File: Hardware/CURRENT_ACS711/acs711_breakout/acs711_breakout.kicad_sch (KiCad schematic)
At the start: 13 parts, among them J1 Conn_01x01, J2 Conn_01x01, J3 Conn_01x04, U1 ACS711xEXLT-15AB

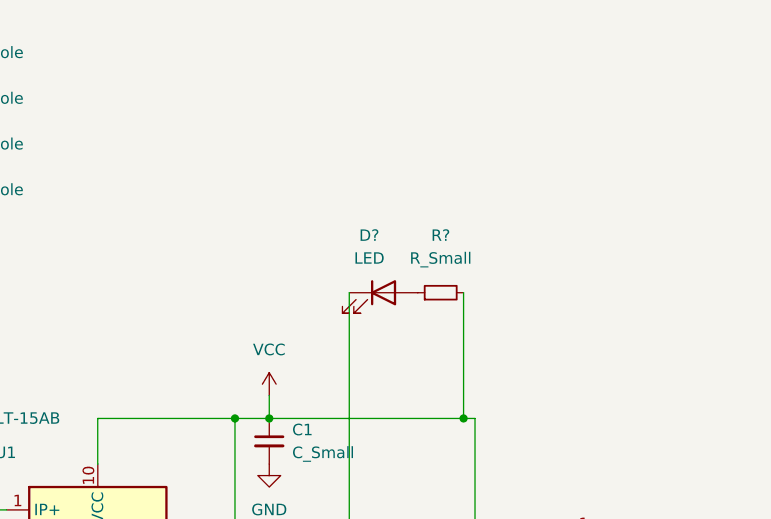
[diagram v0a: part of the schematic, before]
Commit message: layout and some stitching vias
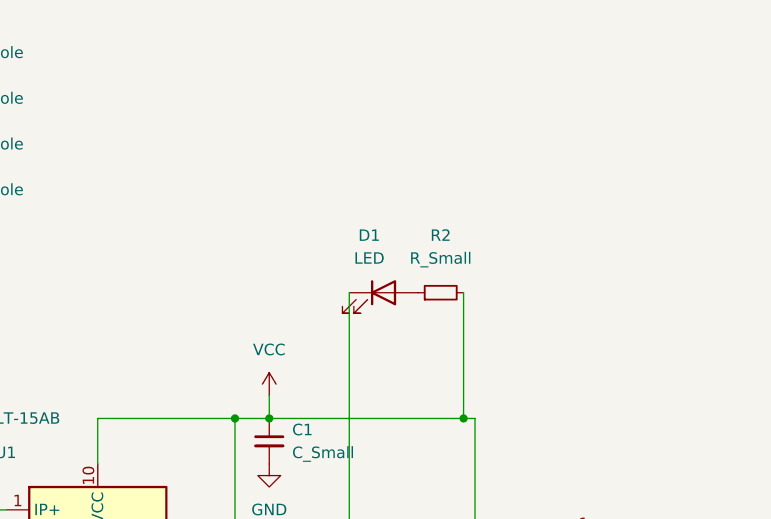
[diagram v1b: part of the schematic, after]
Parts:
- gave numbers to parts that had none: 2
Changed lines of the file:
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@@
   (symbol (lib_id "Device:LED") (at 190.5 62.23 0) (unit 1)
     (in_bom yes) (on_board yes) (fields_autoplaced)
-    (property "Reference" "D?" (id 0) (at 188.9125 55.88 0))
+    (property "Reference" "D1" (id 0) (at 188.9125 55.88 0))
     (property "Value" "LED" (id 1) (at 188.9125 58.42 0))
     (property "Footprint" "LED_SMD:LED_PLCC-2" (id 2) (at 190.5 62.23 0)
@@
   (symbol (lib_id "Device:R_Small") (at 196.85 62.23 90) (unit 1)
     (in_bom yes) (on_board yes) (fields_autoplaced)
-    (property "Reference" "R?" (id 0) (at 196.85 55.88 90))
+    (property "Reference" "R2" (id 0) (at 196.85 55.88 90))
     (property "Value" "R_Small" (id 1) (at 196.85 58.42 90))
     (property "Footprint" "Resistor_SMD:R_0805_2012Metric" (id 2) (at 196.85 62.23 0)
@@
     )
     (path "/af7944d9-46c2-48f3-ab44-3df3aeec04e4"
-      (reference "D?") (unit 1) (value "LED") (footprint "LED_SMD:LED_PLCC-2")
+      (reference "D1") (unit 1) (value "LED") (footprint "LED_SMD:LED_PLCC-2")
     )
     (path "/8c2d72eb-e3f8-4004-bace-d91f46a7cffd"
@@
     )
     (path "/c642f5fe-0d4c-463f-9bd1-b1511f7116d0"
-      (reference "R?") (unit 1) (value "R_Small") (footprint "Resistor_SMD:R_0805_2012Metric")
+      (reference "R2") (unit 1) (value "R_Small") (footprint "Resistor_SMD:R_0805_2012Metric")
     )
     (path "/77d667f7-c52a-418a-9c37-7123db607eaa"

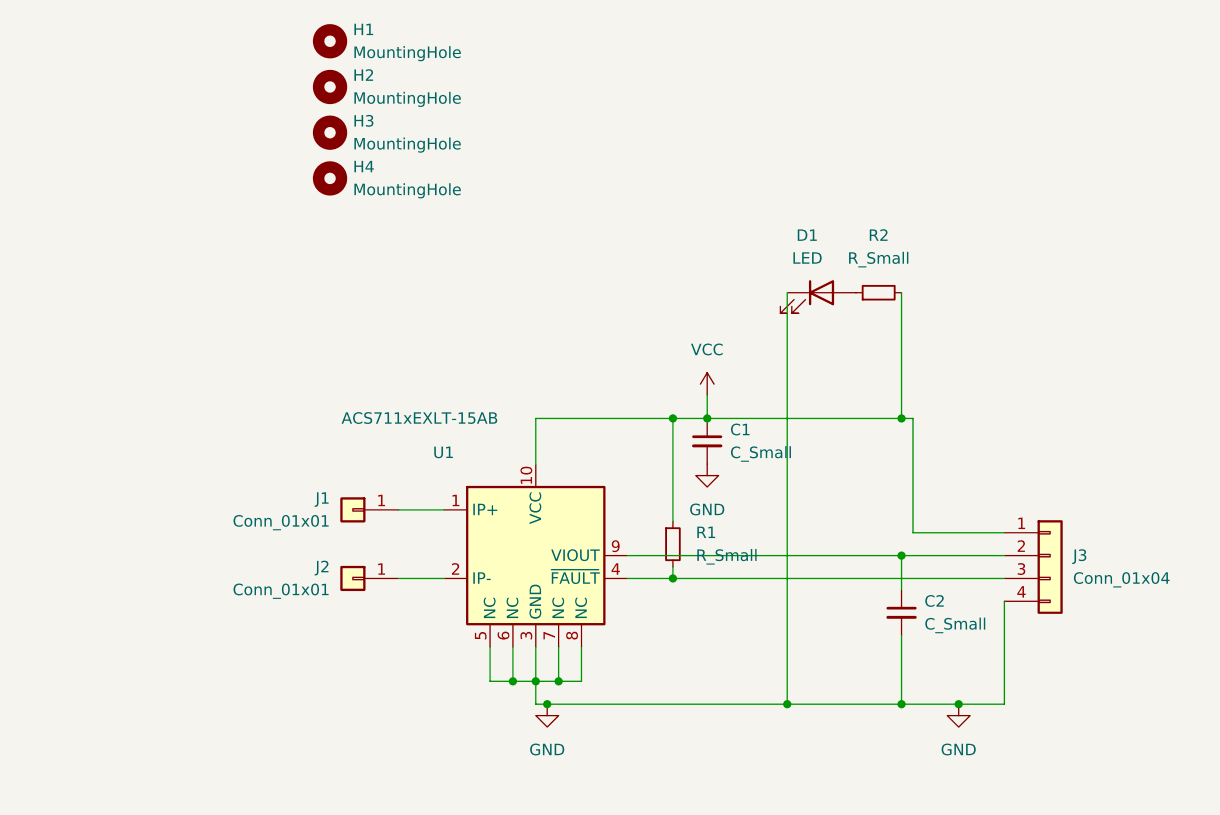
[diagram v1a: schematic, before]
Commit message: Last version of altimeter and ACS7111 pcbs
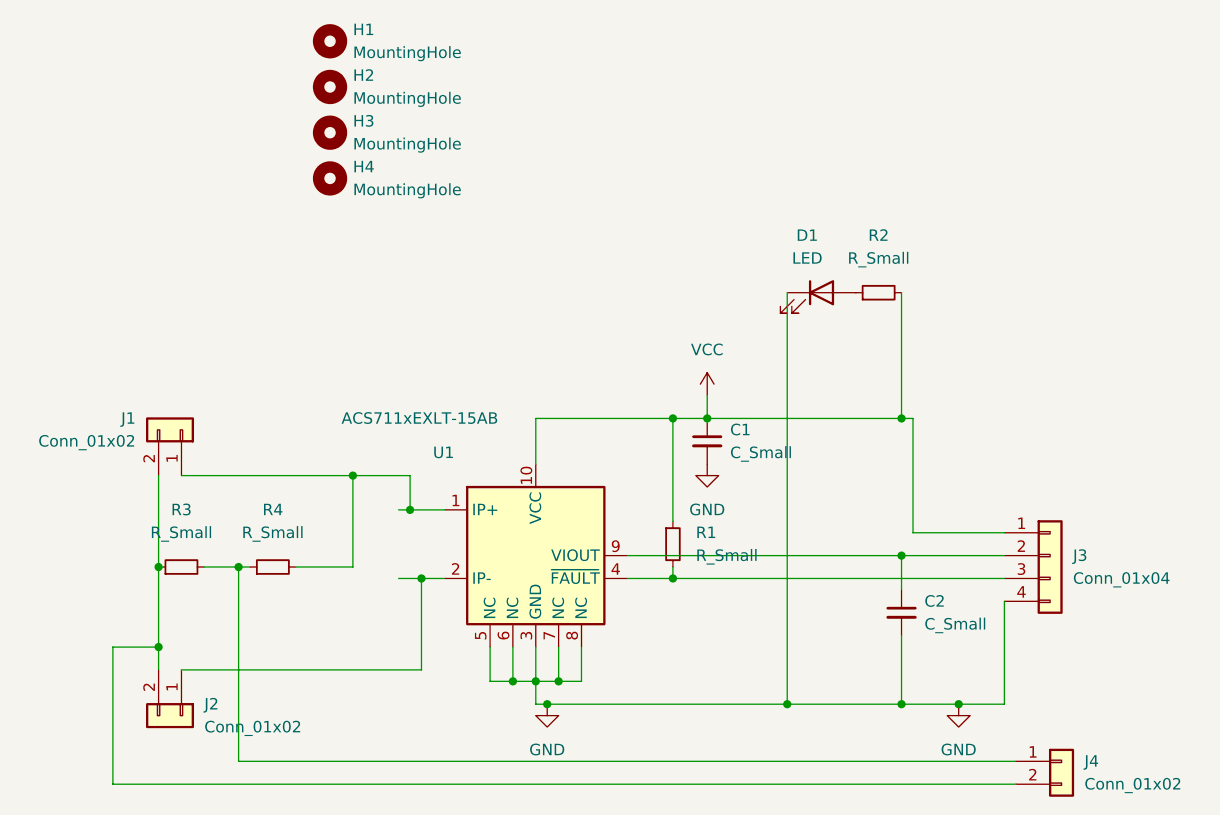
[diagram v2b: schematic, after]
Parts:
- removed J1, J2: Conn_01x01, TestPoint:TestPoint_Pad_4.0x4.0mm, symbol Connector_Generic:Conn_01x01
- added J1: Conn_01x02, Connector_AMASS:AMASS_XT60-M_1x02_P7.20mm_Vertical, symbol Connector_Generic:Conn_01x02
- added J2: Conn_01x02, Connector_AMASS:AMASS_XT60-F_1x02_P7.20mm_Vertical, symbol Connector_Generic:Conn_01x02
- added J4: Conn_01x02, Connector_PinHeader_2.54mm:PinHeader_1x02_P2.54mm_Vertical, symbol Connector_Generic:Conn_01x02
- added R3, R4: R_Small, Resistor_SMD:R_0805_2012Metric, symbol Device:R_Small
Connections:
- net at U1.1 (IP+): now also J1.1 (Pin_1), R4.2
- net at U1.2 (IP-): now also J2.1 (Pin_1)
- new net: J1.2 (Pin_2), J2.2 (Pin_2), J4.2 (Pin_2), R3.1
- new net: J4.1 (Pin_1), R3.2, R4.1
